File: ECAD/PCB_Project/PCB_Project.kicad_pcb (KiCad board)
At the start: 2 copper layers, 80 x 100 mm, 28 parts, among them J1 DIST_MCU, J2 DIST_Power, J3 12V, J304 STEPPER, J401 Conn_01x10, J402 Conn_01x10, J403 Conn_01x02, Q301 NPN

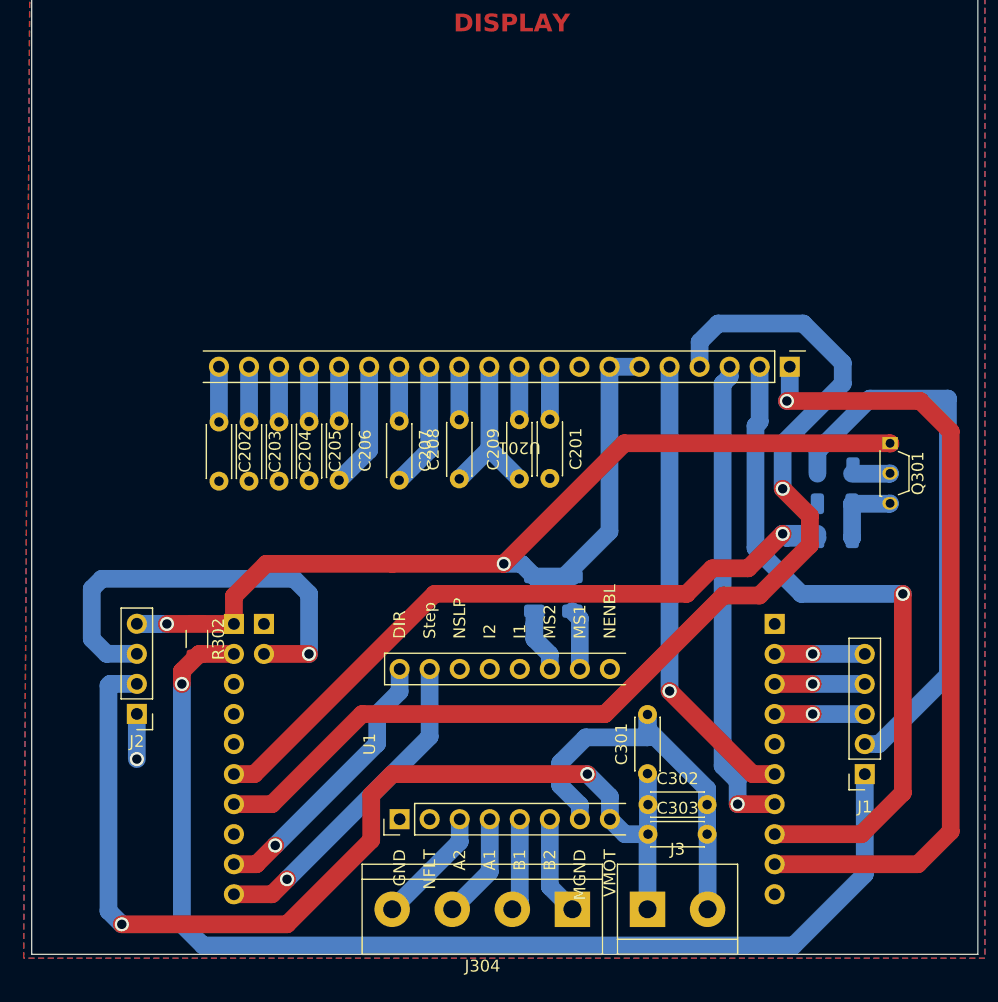
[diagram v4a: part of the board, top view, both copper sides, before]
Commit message: Pushing
COde changes:
MP driver under development
SG90 as well

PCB:
final version, as sent to manufacture

Sims
New sims for report.
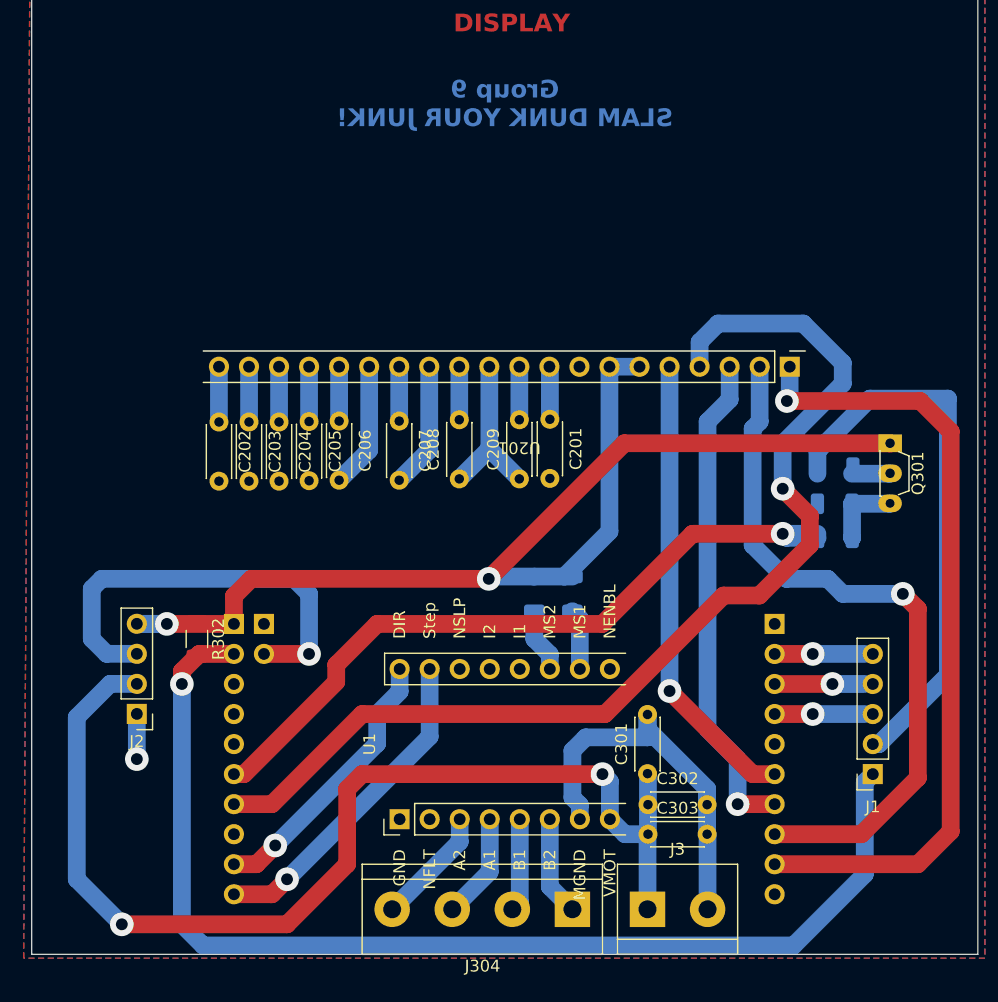
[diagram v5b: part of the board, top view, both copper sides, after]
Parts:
- moved J1 0.68 mm to (173.5, 121.9)
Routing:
- net +12V: track 89.7 -> 94.1 mm
- net /Display/DISPLAY.NRST: track 58.7 -> 59.9 mm
- net /Display/DISPLAY.A0: track 40.9 -> 41.9 mm
- net +3V3: track 101.4 -> 102.3 mm
- net /Sensors + Motor/MGND: track 35.5 -> 34.7 mm
- net /MCU/Ind_Analog: track 60.8 -> 61.7 mm
- net /Sensors + Motor/Inductive_12V: track 47.6 -> 46.9 mm
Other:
- board text added: "Group 9 SLAM DUNK YOUR JUNK!"
